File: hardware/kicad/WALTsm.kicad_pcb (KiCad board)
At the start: 2 copper layers, 40.6 x 50.8 mm, 25 parts, among them J1 JACK_TRRS, P1 CONN_01X06, P2 CONN_01X06, U1 TeensyLC_with_headers, U2 ADXL335, U3 LM321MFX

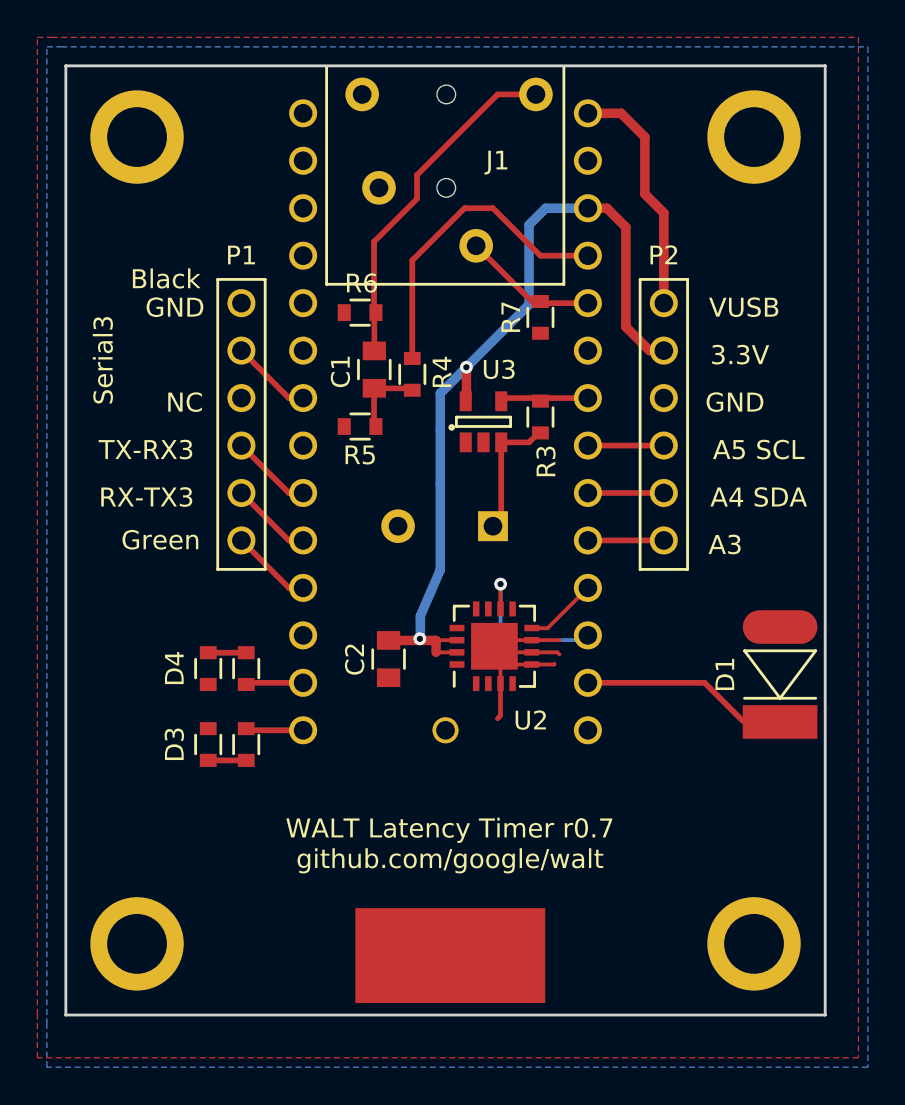
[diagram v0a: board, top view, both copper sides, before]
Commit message: Add a 100 Ohm resistor from TRRS tip to ground
Address #86
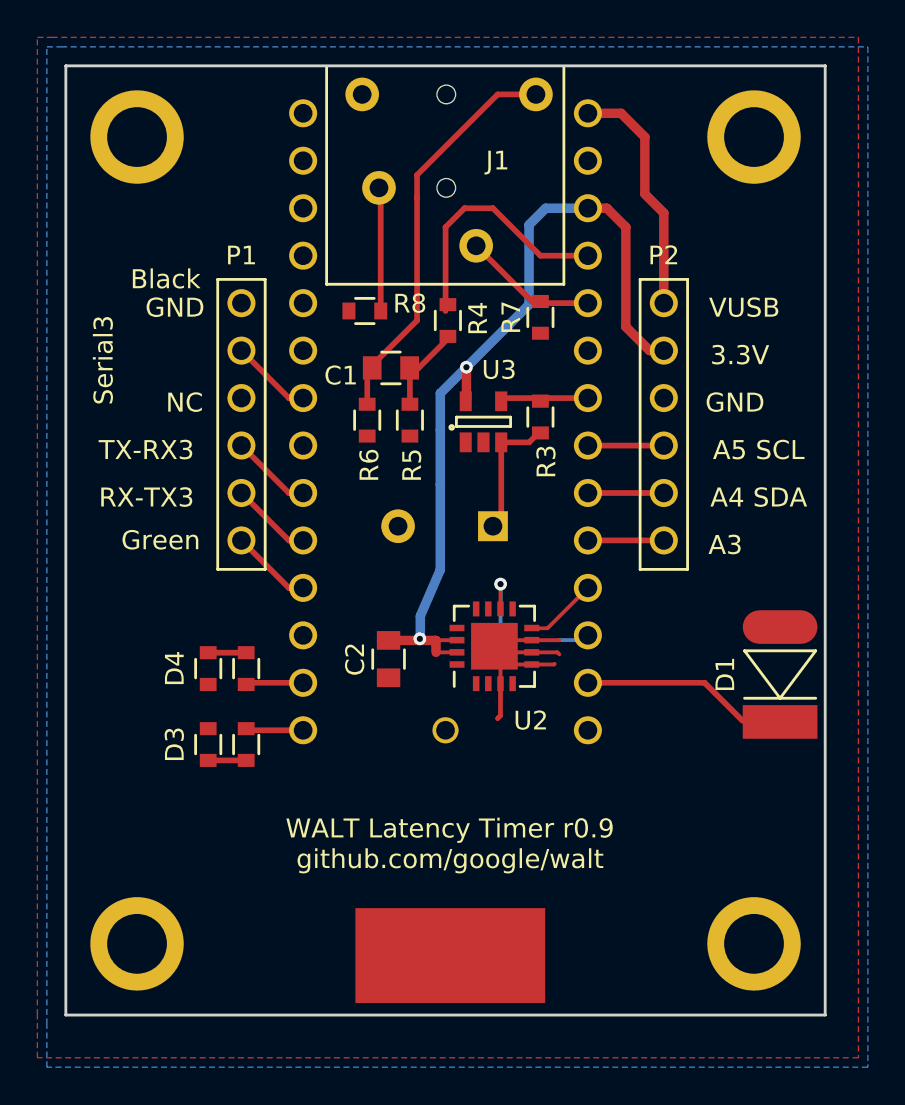
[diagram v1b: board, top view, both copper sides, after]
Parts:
- added R8: 100, walt_footprints:R_0603_pad07mm_long, F.Cu at (82.0, 96.9)
- moved R6 5.77 mm to (82.2, 102.8), turned to 90 degrees
- moved R4 3.45 mm to (86.5, 97.4)
- moved R5 2.69 mm to (84.5, 102.8), turned to 90 degrees
- moved C1 0.89 mm to (83.4, 100.0), turned to 0 degrees
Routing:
- net Net-(J1-Pad2): track 0.00 -> 6.46 mm
- net /MIC_PIN: track 17.0 -> 13.6 mm
- net Net-(C1-Pad1): track 18.5 -> 21.8 mm
- net Net-(C1-Pad2): track 4.08 -> 4.83 mm
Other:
- board text added: "WALT Latency Timer r0.9 github.com/google/walt"
- board text removed: "WALT Latency Timer r0.7 github.com/google/walt"
